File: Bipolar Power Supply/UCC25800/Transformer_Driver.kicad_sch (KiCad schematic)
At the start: 34 parts, among them J1 1715721, T1 750319331, U1 UCC25800-Q1

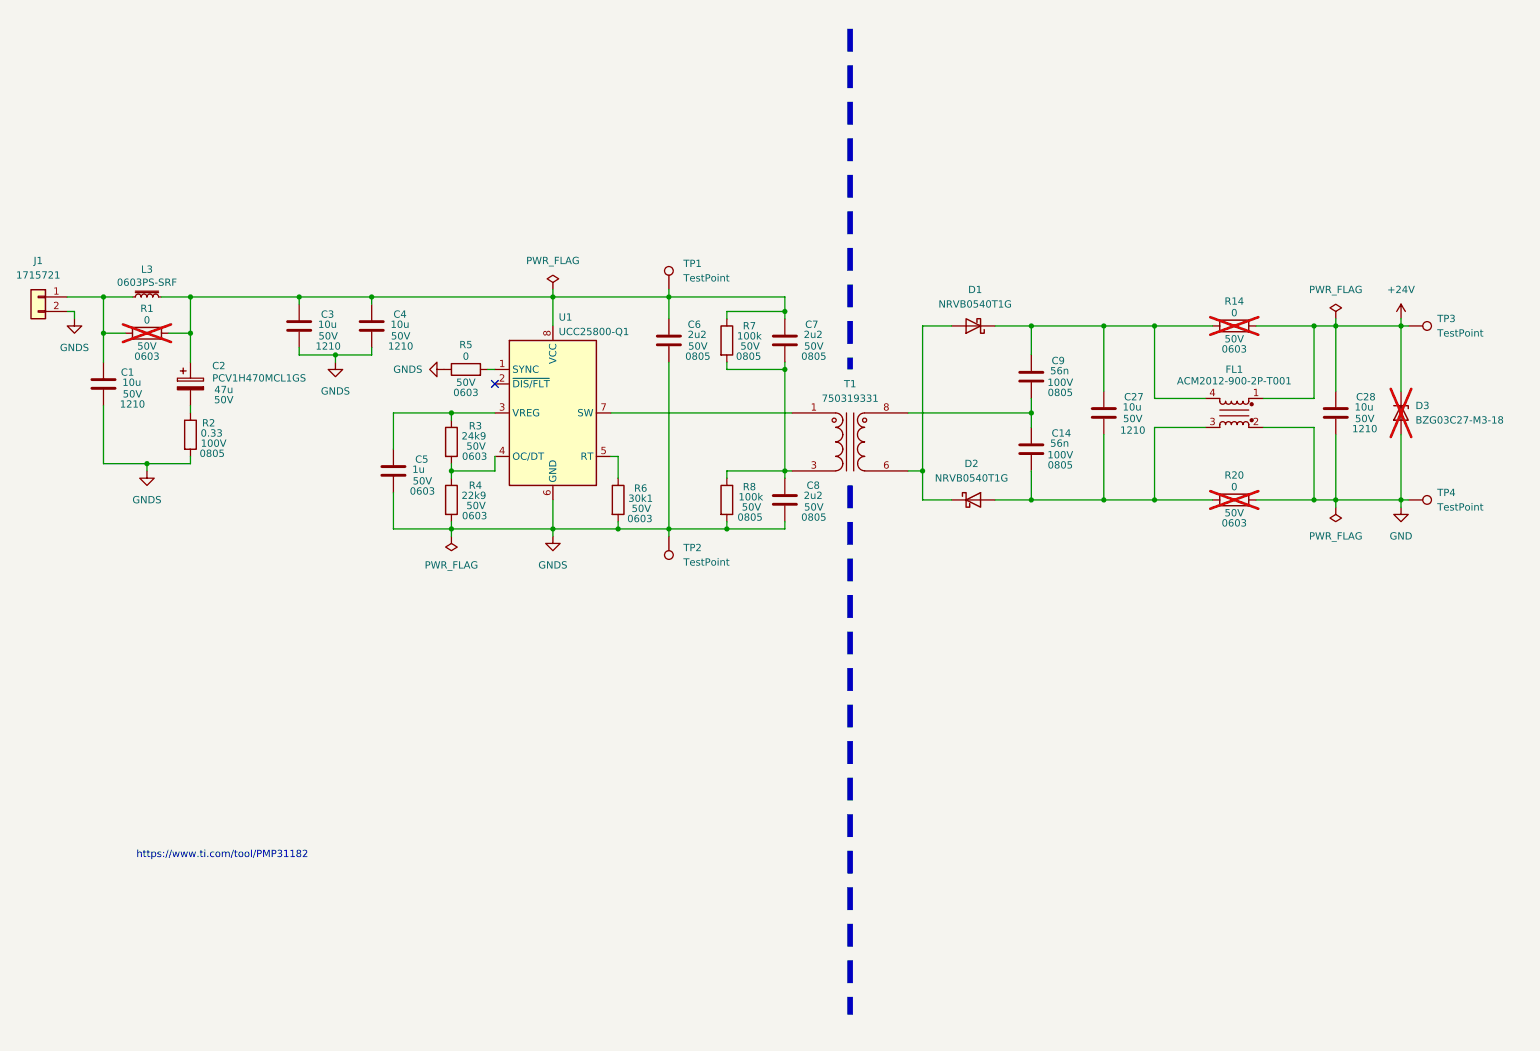
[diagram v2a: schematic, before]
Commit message: BOOST_LT8365 : Design for bipolar 110V supply
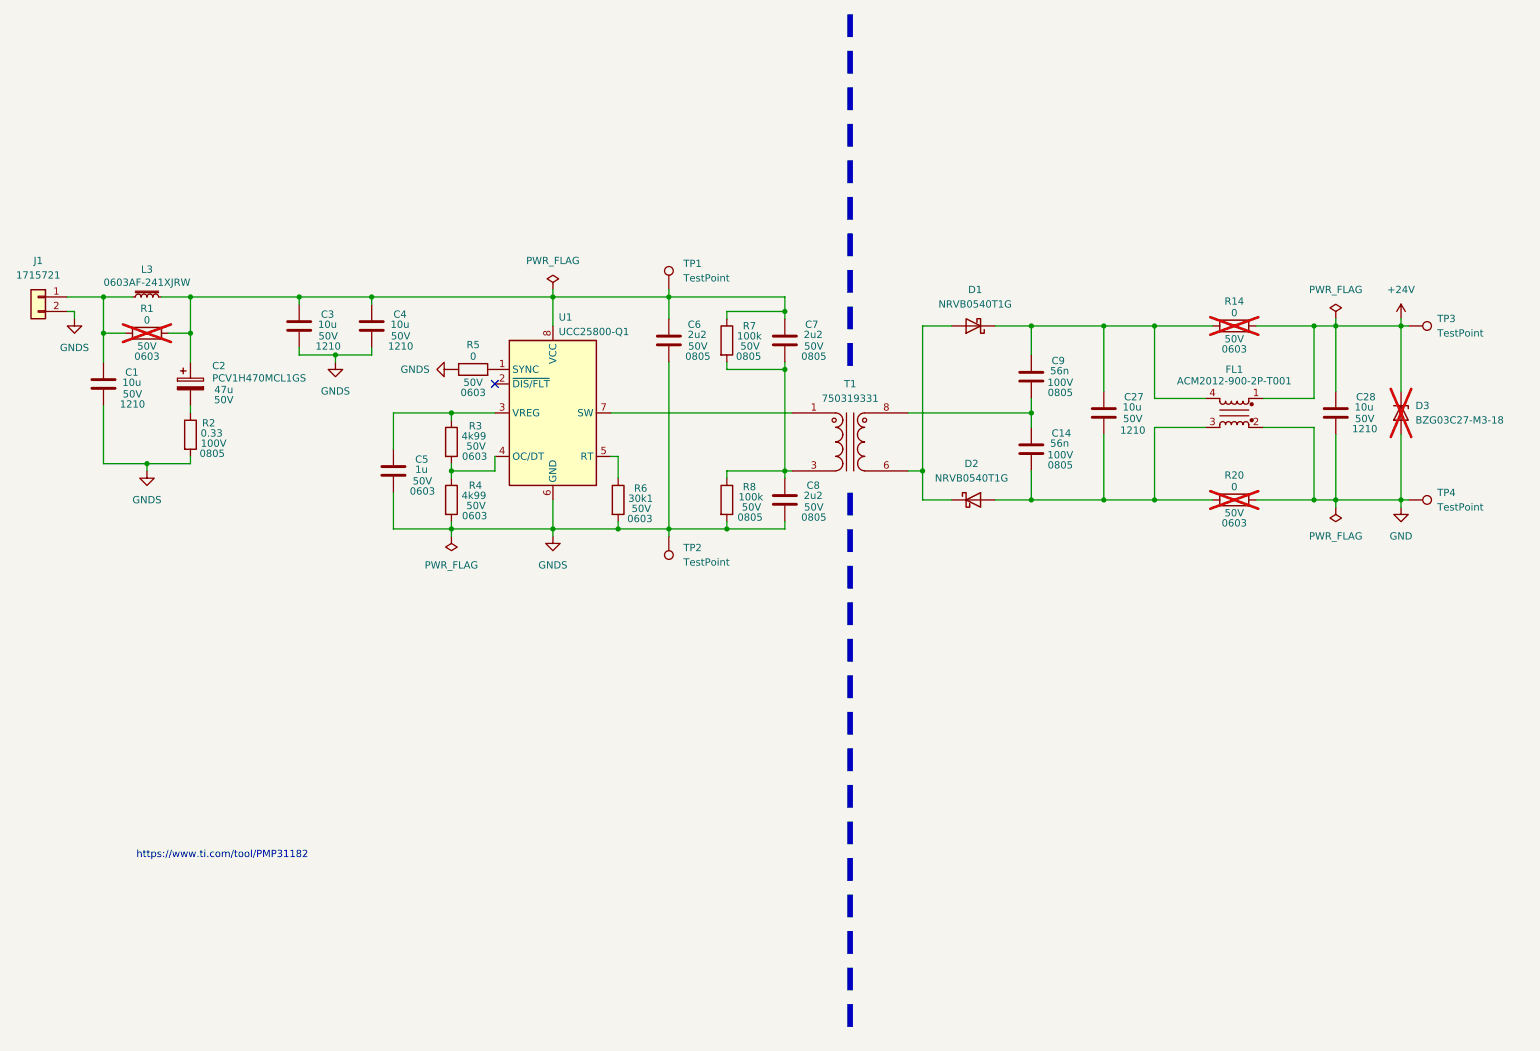
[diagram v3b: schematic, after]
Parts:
- L3: value 0603PS-SRF -> 0603AF-241XJRW
- R3: value 24k9 -> 4k99
- R4: value 22k9 -> 4k99
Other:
- moved on the sheet: R5
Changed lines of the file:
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@@
 	(polyline
 		(pts
-			(xy 162.56 96.52) (xy 162.56 189.23)
+			(xy 162.56 97.79) (xy 162.56 193.04)
 		)
 		(stroke
@@
 	(wire
 		(pts
-			(xy 99.06 76.2) (xy 100.33 76.2)
-		)
-		(stroke
-			(width 0)
-			(type default)
-		)
-	)
-	(wire
-		(pts
 			(xy 92.71 83.82) (xy 82.55 83.82)
 		)
@@
 	(polyline
 		(pts
-			(xy 162.56 16.51) (xy 162.56 76.2)
+			(xy 162.56 13.97) (xy 162.56 76.2)
 		)
 		(stroke
@@
 	(symbol
 		(lib_id "Device:R")
-		(at 95.25 76.2 90)
+		(at 96.52 76.2 90)
 		(unit 1)
 		(exclude_from_sim no)
@@
 		(dnp no)
 		(property "Reference" "R5"
-			(at 95.25 71.882 90)
+			(at 96.52 71.882 90)
 			(effects
 				(font
@@
 		)
 		(property "Value" "0"
-			(at 95.25 73.914 90)
+			(at 96.52 73.914 90)
 			(effects
 				(font
@@
 		)
 		(property "Footprint" "Resistor_SMD:R_0603_1608Metric_Pad0.98x0.95mm_HandSolder"
-			(at 95.25 77.978 90)
+			(at 96.52 77.978 90)
 			(effects
 				(font
@@
 		)
 		(property "Datasheet" "~"
-			(at 95.25 76.2 0)
+			(at 96.52 76.2 0)
 			(effects
 				(font
@@
 		)
 		(property "Description" "Resistor"
-			(at 95.25 76.2 0)
+			(at 96.52 76.2 0)
 			(effects
 				(font
@@
 		)
 		(property "Voltage" "50V"
-			(at 95.25 78.486 90)
+			(at 96.52 78.486 90)
 			(effects
 				(font
@@
 		)
 		(property "Package" "0603"
-			(at 95.25 80.264 90)
+			(at 96.52 80.264 90)
 			(effects
 				(font
@@
 			)
 		)
-		(property "Value" "22k9"
+		(property "Value" "4k99"
 			(at 94.488 98.298 0)
 			(effects
@@
 	(symbol
 		(lib_id "power:GNDS")
-		(at 91.44 76.2 270)
+		(at 92.71 76.2 270)
 		(unit 1)
 		(exclude_from_sim no)
@@
 		(fields_autoplaced yes)
 		(property "Reference" "#PWR04"
-			(at 85.09 76.2 0)
+			(at 86.36 76.2 0)
 			(effects
 				(font
@@
 		)
 		(property "Value" "GNDS"
-			(at 87.63 76.1999 90)
+			(at 88.9 76.1999 90)
 			(effects
 				(font
@@
 		)
 		(property "Footprint" ""
-			(at 91.44 76.2 0)
+			(at 92.71 76.2 0)
 			(effects
 				(font
@@
 		)
 		(property "Datasheet" ""
-			(at 91.44 76.2 0)
+			(at 92.71 76.2 0)
 			(effects
 				(font
@@
 		)
 		(property "Description" "Power symbol creates a global label with name \"GNDS\" , signal ground"
-			(at 91.44 76.2 0)
+			(at 92.71 76.2 0)
 			(effects
 				(font
@@
 		(dnp no)
 		(property "Reference" "C1"
-			(at 34.798 76.708 0)
+			(at 35.56 76.708 0)
 			(effects
 				(font
@@
 			)
 		)
-		(property "Value" "24k9"
+		(property "Value" "4k99"
 			(at 94.488 87.884 0)
 			(effects
@@
 		)
 		(property "Value" "1u"
-			(at 85.852 93.726 0)
+			(at 86.36 93.726 0)
 			(effects
 				(font
@@
 			)
 		)
-		(property "Value" "0603PS-SRF"
+		(property "Value" "0603AF-241XJRW"
 			(at 39.37 60.96 90)
 			(effects
